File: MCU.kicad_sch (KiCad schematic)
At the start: 63 parts, among them IC1 BALFHB-WL-02D3, J13 UART_MAIN, J2 Conn_Coaxial, J3 Led, Q1 S8050, Q2 S8050, SW1 SW_Push, U4 BGS12WN6E6327, U5 STM32WLE5CCUx, Y1 32.768kHz

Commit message: Update schemtic
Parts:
- added R12, R13: 1K, Resistor_SMD:R_0402_1005Metric, symbol Device:R
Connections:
- net PB7 is gone; now on net UART1_RX: U5.5 (PB7)
- net PB0: now also U5.7 (PA0)
- net PB5: now also R19.1; no longer R18.1
- net UART1_RX: now also TP2.1; no longer J13.1 (Pin_1), U5.33 (PA10)
- net UART1_TX: now also TP1.1, U5.4 (PB6); no longer J13.2 (Pin_2), U5.17 (PA9)
- net UART2_RX: now also J13.1 (Pin_1); no longer TP1.1
- net UART2_TX: now also J13.2 (Pin_2); no longer TP2.1
- net PB3: now reaches U5.1 (PB3)
- net PB3: now also R18.1
- net at Q2.2 (E): now also R12.1; no longer J3.1 (Pin_1)
- net at Q1.2 (E): now also R13.1; no longer J3.2 (Pin_2)
- removed net PB6: R19.1, U5.4 (PB6)
- new net: J3.2 (Pin_2), R13.2
- new net: J3.1 (Pin_1), R12.2
- no-connect marks 11 -> 13
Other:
- moved on the sheet: J13, TP1, TP2

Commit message: Update schematic
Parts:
- added R16, R22, R24, R27: 4.7K, Resistor_SMD:R_0402_1005Metric, symbol Device:R
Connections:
- net SDA2 is gone; now on net SCL2: TP6.1, U5.34 (PA11)
- net +3.3V: now also R16.2, R22.2, R24.2, R27.2
- net FE_CTRL1: now also U5.13 (PA5); no longer U5.38 (PC13)
- net SCL2: now also R16.1, R22.1
- net SCL3: now also R27.1
- net SDA3: now also R24.1

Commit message: Update PCB layout
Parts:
- R12, R13: footprint Resistor_SMD:R_0402_1005Metric -> Resistor_SMD:R_0603_1608Metric
- TP1, TP2, TP3, TP4, TP5, TP6: footprint (none) -> TestPoint:TestPoint_Loop_D1.80mm_Drill1.0mm_Beaded
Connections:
- net PB0: no longer U5.7 (PA0)
- net PB3: no longer R18.1
- net SCL2: no longer R16.1, TP6.1, U5.34 (PA11)
- net PB8: now reaches U5.6 (PB8)
- net PB8: now also R18.1
- net PB5: no longer names the net of U5.3 (PB5)
- net PB5: no longer R19.1
- new net PA0: R19.1, U5.7 (PA0)
- new net SDA2: R16.1, TP6.1, U5.34 (PA11)
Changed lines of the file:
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@@
 	)
 	(junction
-		(at 293.37 99.06)
-		(diameter 0)
-		(color 0 0 0 0)
-	)
-	(junction
 		(at 163.83 57.15)
 		(diameter 0)
@@
 	)
 	(no_connect
-		(at 203.2 119.38)
-	)
-	(no_connect
 		(at 256.54 119.38)
 	)
@@
 	)
 	(no_connect
+		(at 203.2 111.76)
+	)
+	(no_connect
 		(at 223.52 147.32)
 	)
@@
 	(wire
 		(pts
+			(xy 201.93 119.38) (xy 203.2 119.38)
+		)
+		(stroke
+			(width 0)
+			(type default)
+		)
+	)
+	(wire
+		(pts
 			(xy 151.13 204.47) (xy 158.75 204.47)
 		)
@@
 	(wire
 		(pts
+			(xy 287.02 101.6) (xy 304.8 101.6)
+		)
+		(stroke
+			(width 0)
+			(type default)
+		)
+	)
+	(wire
+		(pts
+			(xy 191.77 123.19) (xy 201.93 123.19)
+		)
+		(stroke
+			(width 0)
+			(type default)
+		)
+	)
+	(wire
+		(pts
 			(xy 248.92 207.01) (xy 259.08 207.01)
 		)
@@
 	(wire
 		(pts
-			(xy 215.9 90.17) (xy 215.9 93.98)
+			(xy 191.77 120.65) (xy 201.93 120.65)
 		)
 		(stroke
@@
 	(wire
 		(pts
-			(xy 220.98 160.02) (xy 228.6 160.02)
+			(xy 215.9 90.17) (xy 215.9 93.98)
 		)
 		(stroke
@@
 	(wire
 		(pts
-			(xy 293.37 99.06) (xy 293.37 105.41)
+			(xy 220.98 160.02) (xy 228.6 160.02)
 		)
 		(stroke
@@
 	(wire
 		(pts
-			(xy 208.28 90.17) (xy 213.36 90.17)
+			(xy 293.37 99.06) (xy 293.37 105.41)
 		)
 		(stroke
@@
 	(wire
 		(pts
-			(xy 184.15 115.57) (xy 200.66 115.57)
+			(xy 208.28 90.17) (xy 213.36 90.17)
 		)
 		(stroke
@@
 	(wire
 		(pts
-			(xy 293.37 105.41) (xy 307.34 105.41)
+			(xy 184.15 115.57) (xy 200.66 115.57)
 		)
 		(stroke
@@
 	(wire
 		(pts
-			(xy 278.13 88.9) (xy 278.13 90.17)
+			(xy 293.37 105.41) (xy 307.34 105.41)
 		)
 		(stroke
@@
 	(wire
 		(pts
-			(xy 307.34 99.06) (xy 293.37 99.06)
+			(xy 278.13 88.9) (xy 278.13 90.17)
 		)
 		(stroke
@@
 	(wire
 		(pts
-			(xy 201.93 111.76) (xy 203.2 111.76)
-		)
-		(stroke
-			(width 0)
-			(type default)
-		)
-	)
-	(wire
-		(pts
 			(xy 102.87 201.93) (xy 105.41 201.93)
 		)
@@
 	(wire
 		(pts
+			(xy 200.66 106.68) (xy 203.2 106.68)
+		)
+		(stroke
+			(width 0)
+			(type default)
+		)
+	)
+	(wire
+		(pts
 			(xy 199.39 173.99) (xy 195.58 173.99)
 		)
@@
 	(wire
 		(pts
+			(xy 304.8 99.06) (xy 304.8 101.6)
+		)
+		(stroke
+			(width 0)
+			(type default)
+		)
+	)
+	(wire
+		(pts
 			(xy 149.86 111.76) (xy 147.32 111.76)
 		)
@@
 	(wire
 		(pts
-			(xy 287.02 99.06) (xy 287.02 104.14)
+			(xy 287.02 101.6) (xy 287.02 104.14)
 		)
 		(stroke
@@
 	(wire
 		(pts
-			(xy 157.48 132.08) (xy 167.64 132.08)
+			(xy 201.93 123.19) (xy 201.93 121.92)
 		)
 		(stroke
@@
 	(wire
 		(pts
-			(xy 201.93 113.03) (xy 201.93 111.76)
+			(xy 157.48 132.08) (xy 167.64 132.08)
 		)
 		(stroke
@@
 	(wire
 		(pts
-			(xy 195.58 113.03) (xy 201.93 113.03)
+			(xy 307.34 99.06) (xy 304.8 99.06)
 		)
 		(stroke
@@
 	(wire
 		(pts
-			(xy 195.58 106.68) (xy 203.2 106.68)
-		)
-		(stroke
-			(width 0)
-			(type default)
-		)
-	)
-	(wire
-		(pts
 			(xy 220.98 173.99) (xy 210.82 173.99)
 		)
@@
 	(wire
 		(pts
-			(xy 293.37 99.06) (xy 287.02 99.06)
-		)
-		(stroke
-			(width 0)
-			(type default)
-		)
-	)
-	(wire
-		(pts
 			(xy 238.76 80.01) (xy 278.13 80.01)
 		)
@@
 	(wire
 		(pts
-			(xy 199.39 121.92) (xy 203.2 121.92)
-		)
-		(stroke
-			(width 0)
-			(type default)
-		)
-	)
-	(wire
-		(pts
 			(xy 176.53 154.94) (xy 176.53 157.48)
 		)
@@
 	(wire
 		(pts
+			(xy 201.93 120.65) (xy 201.93 119.38)
+		)
+		(stroke
+			(width 0)
+			(type default)
+		)
+	)
+	(wire
+		(pts
 			(xy 330.2 195.58) (xy 330.2 187.96)
 		)
@@
 	(wire
 		(pts
+			(xy 201.93 121.92) (xy 203.2 121.92)
+		)
+		(stroke
+			(width 0)
+			(type default)
+		)
+	)
+	(wire
+		(pts
 			(xy 184.15 105.41) (xy 185.42 105.41)
 		)
@@
 		)
 	)
-	(label "PB5"
+	(label "PA0"
 		(at 261.62 182.88 0)
 		(fields_autoplaced yes)
@@
 		)
 	)
-	(label "PB5"
-		(at 195.58 113.03 0)
+	(label "PA0"
+		(at 191.77 123.19 0)
 		(fields_autoplaced yes)
 		(effects
@@
 		)
 	)
-	(label "PB3"
+	(label "PB8"
 		(at 261.62 175.26 0)
 		(fields_autoplaced yes)
@@
 		)
 	)
-	(label "PB3"
-		(at 195.58 106.68 0)
+	(label "PB8"
+		(at 191.77 120.65 0)
 		(fields_autoplaced yes)
 		(effects
@@
 		)
 	)
-	(hierarchical_label "PB0"
+	(hierarchical_label "PB3"
 		(shape input)
-		(at 199.39 121.92 180)
+		(at 200.66 106.68 180)
 		(fields_autoplaced yes)
 		(effects
@@
 			)
 		)
-		(property "Footprint" ""
+		(property "Footprint" "TestPoint:TestPoint_Loop_D1.80mm_Drill1.0mm_Beaded"
 			(at 190.5 105.41 0)
 			(effects
@@
 			)
 		)
-		(property "Footprint" "Resistor_SMD:R_0402_1005Metric"
+		(property "Footprint" "Resistor_SMD:R_0603_1608Metric"
 			(at 323.85 191.008 90)
 			(effects
@@
 			)
 		)
-		(property "Footprint" ""
+		(property "Footprint" "TestPoint:TestPoint_Loop_D1.80mm_Drill1.0mm_Beaded"
 			(at 176.53 114.3 0)
 			(effects
@@
 			)
 		)
-		(property "Footprint" ""
+		(property "Footprint" "TestPoint:TestPoint_Loop_D1.80mm_Drill1.0mm_Beaded"
 			(at 283.21 99.06 0)
 			(effects
@@
 			)
 		)
-		(property "Footprint" ""
+		(property "Footprint" "TestPoint:TestPoint_Loop_D1.80mm_Drill1.0mm_Beaded"
 			(at 176.53 105.41 0)
 			(effects
@@
 			)
 		)
-		(property "Footprint" "Resistor_SMD:R_0402_1005Metric"
+		(property "Footprint" "Resistor_SMD:R_0603_1608Metric"
 			(at 323.85 197.358 90)
 			(effects
@@
 			)
 		)
-		(property "Footprint" ""
+		(property "Footprint" "TestPoint:TestPoint_Loop_D1.80mm_Drill1.0mm_Beaded"
 			(at 298.45 99.06 0)
 			(effects
@@
 			)
 		)
-		(property "Footprint" ""
+		(property "Footprint" "TestPoint:TestPoint_Loop_D1.80mm_Drill1.0mm_Beaded"
 			(at 203.2 153.67 0)
 			(effects

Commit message: Update antenna
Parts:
- J2: footprint Connector_Coaxial:U.FL_Molex_MCRF_73412-0110_Vertical -> Connector_Coaxial:SMA_Amphenol_132134-11_Vertical
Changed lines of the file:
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@@
 			)
 		)
-		(property "Footprint" "Connector_Coaxial:U.FL_Molex_MCRF_73412-0110_Vertical"
+		(property "Footprint" "Connector_Coaxial:SMA_Amphenol_132134-11_Vertical"
 			(at 78.74 201.93 0)
 			(effects

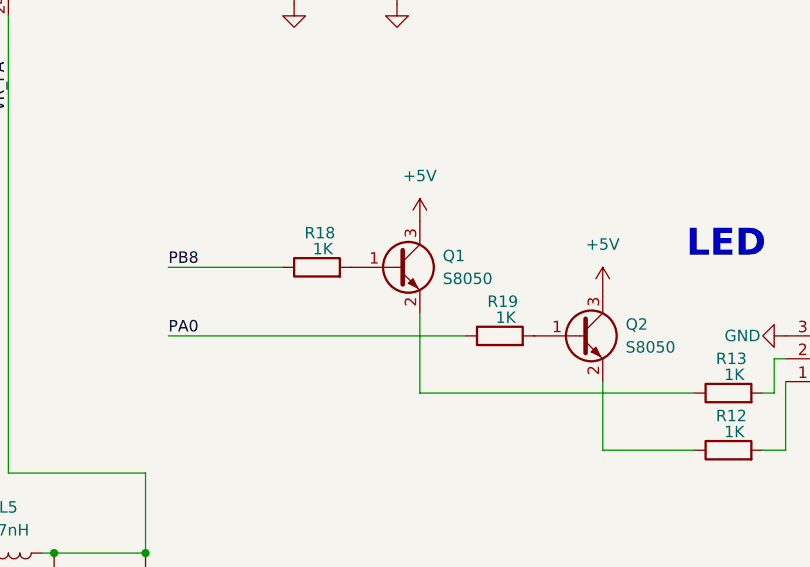
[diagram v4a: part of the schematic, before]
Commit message: Update value resistor and transistor
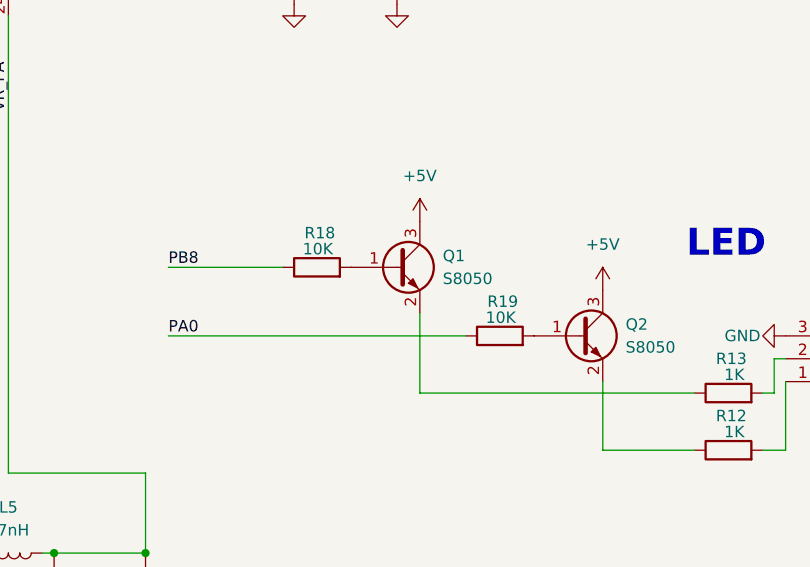
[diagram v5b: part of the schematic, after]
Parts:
- R18, R19: value 1K -> 10K
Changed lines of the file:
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@@
 			)
 		)
-		(property "Value" "1K"
+		(property "Value" "10K"
 			(at 300.228 180.848 90)
 			(effects
@@
 			)
 		)
-		(property "Value" "1K"
+		(property "Value" "10K"
 			(at 279.908 173.228 90)
 			(effects
